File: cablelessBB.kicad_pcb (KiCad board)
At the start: 2 copper layers, 100 x 60 mm, 306 parts

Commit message: del noneed file
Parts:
- moved REF** 20.0 mm to (152.7, 46.1)
- moved REF** 20.0 mm to (152.7, 48.6)
- moved REF** 20.0 mm to (152.7, 38.5)
- moved REF** 20.0 mm to (152.7, 36.0)
- moved REF** 20.0 mm to (152.7, 41.0)
- moved REF** 20.0 mm to (152.7, 43.6)
- moved REF** 20.0 mm to (152.7, 51.2)
- moved REF** 20.0 mm to (155.2, 51.2)
- moved REF** 20.0 mm to (155.2, 43.6)
- moved REF** 20.0 mm to (155.2, 41.0)
- moved REF** 20.0 mm to (155.2, 36.0)
- moved REF** 20.0 mm to (155.2, 38.5)
- moved REF** 20.0 mm to (155.2, 48.6)
- moved REF** 20.0 mm to (155.2, 46.1)
- moved REF** 20.0 mm to (155.2, 63.9)
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
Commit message: 配線1
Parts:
- removed the REF** at (159.0, 72.8)
- removed the REF** at (161.5, 65.2)
- removed the REF** at (174.2, 32.1)
- removed the REF** at (174.2, 41.0)
- removed the REF** at (174.2, 48.6)
- removed the REF** at (174.2, 44.8)
- removed the REF** at (174.2, 51.3)
- removed the REF** at (174.2, 28.3)
- removed the REF** at (176.8, 28.3)
- removed the REF** at (176.8, 51.3)
- removed the REF** at (176.8, 44.8)
- removed the REF** at (176.8, 48.6)
- removed the REF** at (161.5, 61.4)
- removed the REF** at (176.8, 41.0)
- removed the REF** at (216.5, 58.8)
- removed the REF** at (216.5, 61.4)
- removed the REF** at (216.5, 66.4)
- removed the REF** at (216.5, 63.9)
- removed the REF** at (216.5, 74.0)
- removed the REF** at (216.5, 71.5)
- removed the REF** at (216.5, 69.0)
- removed the REF** at (216.5, 46.1)
- removed the REF** at (216.5, 48.6)
- removed the REF** at (161.5, 69.0)
- removed the REF** at (216.5, 51.2)
- removed the REF** at (216.5, 41.0)
- removed the REF** at (216.5, 43.6)
- removed the REF** at (216.5, 38.5)
- removed the REF** at (188.6, 51.2)
- removed the REF** at (188.6, 48.6)
- removed the REF** at (188.6, 44.8)
- removed the REF** at (188.6, 37.2)
- removed the REF** at (188.6, 41.0)
- removed the REF** at (188.6, 32.1)
- removed the REF** at (161.5, 77.9)
- removed the REF** at (201.3, 28.3)
- removed the REF** at (191.1, 41.0)
- removed the REF** at (191.1, 44.8)
- removed the REF** at (191.1, 48.6)
- removed the REF** at (191.1, 51.2)
- removed the REF** at (203.8, 28.3)
- removed the REF** at (191.1, 32.1)
- removed the REF** at (191.1, 37.2)
- removed the REF** at (196.2, 37.2)
- removed the REF** at (196.2, 32.1)
- removed the REF** at (161.5, 72.8)
- removed the REF** at (196.2, 51.2)
- removed the REF** at (196.2, 48.6)
- removed the REF** at (196.2, 44.8)
- removed the REF** at (196.2, 41.0)
- removed the REF** at (193.7, 32.1)
- removed the REF** at (193.7, 41.0)
- removed the REF** at (193.7, 37.2)
- removed the REF** at (193.7, 44.8)
- removed the REF** at (193.7, 48.6)
- removed the REF** at (193.7, 51.2)
- removed the REF** at (166.6, 72.8)
- removed the REF** at (203.8, 51.2)
- removed the REF** at (203.8, 48.6)
- removed the REF** at (203.8, 44.8)
- removed the REF** at (203.8, 37.2)
- removed the REF** at (203.8, 41.0)
- removed the REF** at (203.8, 32.1)
- removed the REF** at (206.4, 41.0)
- removed the REF** at (206.4, 44.8)
- removed the REF** at (206.4, 48.6)
- removed the REF** at (206.4, 51.2)
- removed the REF** at (166.6, 77.9)
- removed the REF** at (206.4, 28.3)
- removed the REF** at (206.4, 32.1)
- removed the REF** at (206.4, 37.2)
- removed the REF** at (201.3, 37.2)
- removed the REF** at (201.3, 32.1)
- removed the REF** at (201.3, 51.2)
- removed the REF** at (201.3, 48.6)
- removed the REF** at (201.3, 44.8)
- removed the REF** at (201.3, 41.0)
- removed the REF** at (198.7, 32.1)
- removed the REF** at (166.6, 69.0)
- removed the REF** at (198.7, 41.0)
- removed the REF** at (198.7, 37.2)
- removed the REF** at (198.7, 44.8)
- removed the REF** at (198.7, 48.6)
- removed the REF** at (198.7, 51.2)
- removed the REF** at (191.1, 28.3)
- removed the REF** at (193.7, 28.3)
- removed the REF** at (186.0, 37.2)
- removed the REF** at (186.0, 32.1)
- removed the REF** at (198.7, 28.3)
- removed the REF** at (166.6, 61.4)
- removed the REF** at (186.0, 51.2)
- removed the REF** at (186.0, 48.6)
- removed the REF** at (186.0, 44.8)
- removed the REF** at (186.0, 41.0)
- removed the REF** at (196.2, 28.3)
- removed the REF** at (183.5, 32.1)
- removed the REF** at (183.5, 41.0)
- removed the REF** at (183.5, 37.2)
- removed the REF** at (183.5, 44.8)
- removed the REF** at (183.5, 48.6)
- removed the REF** at (166.6, 65.2)
- removed the REF** at (183.5, 51.2)
- removed the REF** at (186.0, 28.3)
- removed the REF** at (188.6, 28.3)
- removed the REF** at (183.5, 28.3)
- removed the REF** at (188.6, 76.6)
- removed the REF** at (188.6, 80.4)
- removed the REF** at (191.1, 80.4)
- removed the REF** at (191.1, 76.6)
- removed the REF** at (196.2, 76.6)
- removed the REF** at (196.2, 80.4)
- removed the REF** at (159.0, 77.9)
- removed the REF** at (166.6, 58.7)
- removed the REF** at (193.7, 80.4)
- removed the REF** at (193.7, 76.6)
- removed the REF** at (203.8, 76.6)
- removed the REF** at (203.8, 80.4)
- removed the REF** at (206.4, 80.4)
- removed the REF** at (206.4, 76.6)
- removed the REF** at (201.3, 76.6)
- removed the REF** at (201.3, 80.4)
- removed the REF** at (198.7, 80.4)
- removed the REF** at (198.7, 76.6)
- removed the REF** at (166.6, 81.7)
- removed the REF** at (186.0, 76.6)
- removed the REF** at (186.0, 80.4)
- removed the REF** at (183.5, 80.4)
- removed the REF** at (183.5, 76.6)
- removed the REF** at (188.6, 58.8)
- removed the REF** at (188.6, 61.4)
- removed the REF** at (164.1, 81.7)
- removed the REF** at (188.6, 65.2)
- removed the REF** at (188.6, 72.8)
- removed the REF** at (188.6, 69.0)
- removed the REF** at (191.1, 69.0)
- removed the REF** at (191.1, 72.8)
- removed the REF** at (191.1, 65.2)
- removed the REF** at (191.1, 61.4)
- removed the REF** at (191.1, 58.8)
- removed the REF** at (196.2, 58.8)
- removed the REF** at (196.2, 61.4)
- removed the REF** at (164.1, 58.7)
- removed the REF** at (196.2, 65.2)
- removed the REF** at (196.2, 72.8)
- removed the REF** at (196.2, 69.0)
- removed the REF** at (193.7, 69.0)
- removed the REF** at (193.7, 72.8)
- removed the REF** at (193.7, 65.2)
- removed the REF** at (193.7, 61.4)
- removed the REF** at (193.7, 58.8)
- removed the REF** at (203.8, 58.8)
- removed the REF** at (203.8, 61.4)
- removed the REF** at (164.1, 65.2)
- removed the REF** at (203.8, 65.2)
- removed the REF** at (203.8, 72.8)
- removed the REF** at (203.8, 69.0)
- removed the REF** at (206.4, 69.0)
- removed the REF** at (206.4, 72.8)
- removed the REF** at (206.4, 65.2)
- removed the REF** at (206.4, 61.4)
- removed the REF** at (206.4, 58.8)
- removed the REF** at (201.3, 58.8)
- removed the REF** at (201.3, 61.4)
- removed the REF** at (164.1, 61.4)
- removed the REF** at (201.3, 65.2)
- removed the REF** at (201.3, 72.8)
- removed the REF** at (201.3, 69.0)
- removed the REF** at (198.7, 69.0)
- removed the REF** at (198.7, 72.8)
- removed the REF** at (198.7, 65.2)
- removed the REF** at (198.7, 61.4)
- removed the REF** at (198.7, 58.8)
- removed the REF** at (186.0, 58.8)
- removed the REF** at (186.0, 61.4)
- removed the REF** at (164.1, 69.0)
- removed the REF** at (186.0, 65.2)
- removed the REF** at (186.0, 72.8)
- removed the REF** at (186.0, 69.0)
- removed the REF** at (183.5, 69.0)
- removed the REF** at (183.5, 72.8)
- removed the REF** at (183.5, 65.2)
- removed the REF** at (183.5, 61.4)
- removed the REF** at (183.5, 58.8)
- removed the REF** at (216.5, 36.0)
- removed the REF** at (152.7, 46.1)
- removed the REF** at (164.1, 77.9)
- removed the REF** at (152.7, 48.6)
- removed the REF** at (152.7, 38.5)
- removed the REF** at (152.7, 36.0)
- removed the REF** at (152.7, 41.0)
- removed the REF** at (152.7, 43.6)
- removed the REF** at (152.7, 51.2)
- removed the REF** at (155.2, 51.2)
- removed the REF** at (155.2, 43.6)
- removed the REF** at (155.2, 41.0)
- removed the REF** at (155.2, 36.0)
- removed the REF** at (164.1, 72.8)
- removed the REF** at (155.2, 38.5)
- removed the REF** at (155.2, 48.6)
- removed the REF** at (155.2, 46.1)
- removed the REF** at (155.2, 63.9)
- removed the REF** at (155.2, 61.4)
- removed the REF** at (155.2, 71.5)
- removed the REF** at (155.2, 74.0)
- removed the REF** at (155.2, 69.0)
- removed the REF** at (155.2, 66.4)
- removed the REF** at (155.2, 58.8)
- removed the REF** at (174.2, 72.8)
- removed the REF** at (152.7, 58.8)
- removed the REF** at (152.7, 66.4)
- removed the REF** at (152.7, 69.0)
- removed the REF** at (152.7, 74.0)
- removed the REF** at (152.7, 71.5)
- removed the REF** at (152.7, 61.4)
- removed the REF** at (152.7, 63.9)
- removed the REF** at (152.7, 33.4)
- removed the REF** at (152.7, 30.9)
- removed the REF** at (155.2, 30.9)
- removed the REF** at (159.0, 69.0)
- removed the REF** at (174.2, 77.9)
- removed the REF** at (155.2, 33.4)
- removed the REF** at (155.2, 76.6)
- removed the REF** at (155.2, 79.1)
- removed the REF** at (152.7, 79.1)
- removed the REF** at (152.7, 76.6)
- removed the REF** at (176.8, 32.1)
- removed the REF** at (176.8, 37.2)
- removed the REF** at (174.2, 69.0)
- removed the REF** at (174.2, 61.4)
- removed the REF** at (174.2, 65.2)
- removed the REF** at (174.2, 58.7)
- removed the REF** at (174.2, 81.7)
- removed the REF** at (176.8, 81.7)
- removed the REF** at (176.8, 58.7)
- removed the REF** at (176.8, 65.2)
- removed the REF** at (176.8, 61.4)
- removed the REF** at (159.0, 61.4)
- removed the REF** at (176.8, 69.0)
- removed the REF** at (176.8, 77.9)
- removed the REF** at (176.8, 72.8)
- removed the REF** at (171.7, 72.8)
- removed the REF** at (171.7, 77.9)
- removed the REF** at (171.7, 69.0)
- removed the REF** at (171.7, 61.4)
- removed the REF** at (171.7, 65.2)
- removed the REF** at (171.7, 58.7)
- removed the REF** at (171.7, 81.7)
- removed the REF** at (159.0, 65.2)
- removed the REF** at (169.1, 81.7)
- removed the REF** at (169.1, 58.7)
- removed the REF** at (169.1, 65.2)
- removed the REF** at (169.1, 61.4)
- removed the REF** at (169.1, 69.0)
- removed the REF** at (169.1, 77.9)
- removed the REF** at (169.1, 72.8)
- removed the REF** at (166.6, 37.2)
- removed the REF** at (166.6, 32.1)
- removed the REF** at (166.6, 41.0)
- removed the REF** at (159.0, 58.7)
- removed the REF** at (166.6, 48.6)
- removed the REF** at (166.6, 44.8)
- removed the REF** at (166.6, 51.3)
- removed the REF** at (166.6, 28.3)
- removed the REF** at (164.1, 28.3)
- removed the REF** at (164.1, 51.3)
- removed the REF** at (164.1, 44.8)
- removed the REF** at (164.1, 48.6)
- removed the REF** at (164.1, 41.0)
- removed the REF** at (164.1, 32.1)
- removed the REF** at (159.0, 81.7)
- removed the REF** at (164.1, 37.2)
- removed the REF** at (159.0, 37.2)
- removed the REF** at (159.0, 32.1)
- removed the REF** at (159.0, 41.0)
- removed the REF** at (159.0, 48.6)
- removed the REF** at (159.0, 44.8)
- removed the REF** at (159.0, 51.3)
- removed the REF** at (159.0, 28.3)
- removed the REF** at (161.5, 28.3)
- removed the REF** at (161.5, 51.3)
- removed the REF** at (161.5, 81.7)
- removed the REF** at (161.5, 44.8)
- removed the REF** at (161.5, 48.6)
- removed the REF** at (161.5, 41.0)
- removed the REF** at (161.5, 32.1)
- removed the REF** at (161.5, 37.2)
- removed the REF** at (171.7, 37.2)
- removed the REF** at (171.7, 32.1)
- removed the REF** at (171.7, 41.0)
- removed the REF** at (171.7, 48.6)
- removed the REF** at (171.7, 44.8)
- removed the REF** at (161.5, 58.7)
- removed the REF** at (171.7, 51.3)
- removed the REF** at (171.7, 28.3)
- removed the REF** at (169.1, 28.3)
- removed the REF** at (169.1, 51.3)
- removed the REF** at (169.1, 44.8)
- removed the REF** at (169.1, 48.6)
- removed the REF** at (169.1, 41.0)
- removed the REF** at (169.1, 32.1)
- removed the REF** at (169.1, 37.2)
- removed the REF** at (174.2, 37.2)
- added JP1: Jumper_NO_Small, lib:jump, F.Cu at (110.2, 55.5)
- added JP10: Jumper_NO_Small, lib:jump, F.Cu at (110.2, 124.1)
- added JP100: Jumper_NO_Small, lib:jump, F.Cu at (125.4, 63.2)
- added JP101: Jumper_NO_Small, lib:jump, F.Cu at (125.4, 65.7)
- added JP102: Jumper_NO_Small, lib:jump, F.Cu at (125.4, 68.2)
- added JP103: Jumper_NO_Small, lib:jump, F.Cu at (125.4, 75.9)
- added JP104: Jumper_NO_Small, lib:jump, F.Cu at (125.4, 81.0)
- added JP105: Jumper_NO_Small, lib:jump, F.Cu at (125.4, 119.0)
- added JP106: Jumper_NO_Small, lib:jump, F.Cu at (125.4, 124.1)
- added JP107: Jumper_NO_Small, lib:jump, F.Cu at (125.4, 131.8)
- added JP108: Jumper_NO_Small, lib:jump, F.Cu at (125.4, 134.3)
- added JP109: Jumper_NO_Small, lib:jump, F.Cu at (125.4, 136.8)
- added JP11: Jumper_NO_Small, lib:jump, F.Cu at (110.2, 131.8)
- added JP110: Jumper_NO_Small, lib:jump, F.Cu at (125.4, 139.4)
- added JP111: Jumper_NO_Small, lib:jump, F.Cu at (125.4, 141.9)
- added JP112: Jumper_NO_Small, lib:jump, F.Cu at (125.4, 144.4)
- added JP113: Jumper_NO_Small, lib:jump, F.Cu at (127.9, 55.5)
- added JP114: Jumper_NO_Small, lib:jump, F.Cu at (127.9, 58.1)
- added JP115: Jumper_NO_Small, lib:jump, F.Cu at (127.9, 60.6)
- added JP116: Jumper_NO_Small, lib:jump, F.Cu at (127.9, 63.2)
- added JP117: Jumper_NO_Small, lib:jump, F.Cu at (127.9, 65.7)
- added JP118: Jumper_NO_Small, lib:jump, F.Cu at (127.9, 68.2)
- added JP119: Jumper_NO_Small, lib:jump, F.Cu at (127.9, 75.9)
- added JP12: Jumper_NO_Small, lib:jump, F.Cu at (110.2, 134.3)
- added JP120: Jumper_NO_Small, lib:jump, F.Cu at (127.9, 81.0)
- added JP121: Jumper_NO_Small, lib:jump, F.Cu at (127.9, 119.0)
- added JP122: Jumper_NO_Small, lib:jump, F.Cu at (127.9, 124.1)
- added JP123: Jumper_NO_Small, lib:jump, F.Cu at (127.9, 131.8)
- added JP124: Jumper_NO_Small, lib:jump, F.Cu at (127.9, 134.3)
- added JP125: Jumper_NO_Small, lib:jump, F.Cu at (127.9, 136.8)
- added JP126: Jumper_NO_Small, lib:jump, F.Cu at (127.9, 139.4)
- added JP127: Jumper_NO_Small, lib:jump, F.Cu at (127.9, 141.9)
- added JP128: Jumper_NO_Small, lib:jump, F.Cu at (127.9, 144.4)
- added JP129: Jumper_NO_Small, lib:jump, F.Cu at (130.5, 55.5)
- added JP13: Jumper_NO_Small, lib:jump, F.Cu at (110.2, 136.8)
- added JP130: Jumper_NO_Small, lib:jump, F.Cu at (130.5, 58.1)
- added JP131: Jumper_NO_Small, lib:jump, F.Cu at (130.5, 60.6)
- added JP132: Jumper_NO_Small, lib:jump, F.Cu at (130.5, 63.2)
- added JP133: Jumper_NO_Small, lib:jump, F.Cu at (130.5, 65.7)
- added JP134: Jumper_NO_Small, lib:jump, F.Cu at (130.5, 68.2)
- added JP135: Jumper_NO_Small, lib:jump, F.Cu at (130.5, 75.9)
- added JP136: Jumper_NO_Small, lib:jump, F.Cu at (130.5, 81.0)
- added JP137: Jumper_NO_Small, lib:jump, F.Cu at (130.5, 119.0)
- added JP138: Jumper_NO_Small, lib:jump, F.Cu at (130.5, 124.1)
- added JP139: Jumper_NO_Small, lib:jump, F.Cu at (130.5, 131.8)
- added JP14: Jumper_NO_Small, lib:jump, F.Cu at (110.2, 139.4)
- added JP140: Jumper_NO_Small, lib:jump, F.Cu at (130.5, 134.3)
- added JP141: Jumper_NO_Small, lib:jump, F.Cu at (130.5, 136.8)
- added JP142: Jumper_NO_Small, lib:jump, F.Cu at (130.5, 139.4)
- added JP143: Jumper_NO_Small, lib:jump, F.Cu at (130.5, 141.9)
- added JP144: Jumper_NO_Small, lib:jump, F.Cu at (130.5, 144.4)
- added JP145: Jumper_NO_Small, lib:jump, F.Cu at (133.0, 55.5)
- added JP146: Jumper_NO_Small, lib:jump, F.Cu at (133.0, 58.1)
- added JP147: Jumper_NO_Small, lib:jump, F.Cu at (133.0, 60.6)
- added JP148: Jumper_NO_Small, lib:jump, F.Cu at (133.0, 63.2)
- added JP149: Jumper_NO_Small, lib:jump, F.Cu at (133.0, 65.7)
- added JP15: Jumper_NO_Small, lib:jump, F.Cu at (110.2, 141.9)
- added JP150: Jumper_NO_Small, lib:jump, F.Cu at (133.0, 68.2)
- added JP151: Jumper_NO_Small, lib:jump, F.Cu at (133.0, 75.9)
- added JP152: Jumper_NO_Small, lib:jump, F.Cu at (133.0, 81.0)
- added JP153: Jumper_NO_Small, lib:jump, F.Cu at (133.0, 119.0)
- added JP154: Jumper_NO_Small, lib:jump, F.Cu at (133.0, 124.1)
- added JP155: Jumper_NO_Small, lib:jump, F.Cu at (133.0, 131.8)
- added JP156: Jumper_NO_Small, lib:jump, F.Cu at (133.0, 134.3)
- added JP157: Jumper_NO_Small, lib:jump, F.Cu at (133.0, 136.8)
- added JP158: Jumper_NO_Small, lib:jump, F.Cu at (133.0, 139.4)
- added JP159: Jumper_NO_Small, lib:jump, F.Cu at (133.0, 141.9)
- added JP16: Jumper_NO_Small, lib:jump, F.Cu at (110.2, 144.4)
- added JP160: Jumper_NO_Small, lib:jump, F.Cu at (133.0, 144.4)
- added JP161: Jumper_NO_Small, lib:jump, F.Cu at (135.6, 55.5)
- added JP162: Jumper_NO_Small, lib:jump, F.Cu at (135.6, 58.1)
- added JP163: Jumper_NO_Small, lib:jump, F.Cu at (135.6, 60.6)
- added JP164: Jumper_NO_Small, lib:jump, F.Cu at (135.6, 63.2)
- added JP165: Jumper_NO_Small, lib:jump, F.Cu at (135.6, 65.7)
- added JP166: Jumper_NO_Small, lib:jump, F.Cu at (135.6, 68.2)
- added JP167: Jumper_NO_Small, lib:jump, F.Cu at (135.6, 75.9)
- added JP168: Jumper_NO_Small, lib:jump, F.Cu at (135.6, 81.0)
- added JP169: Jumper_NO_Small, lib:jump, F.Cu at (135.6, 119.0)
- added JP17: Jumper_NO_Small, lib:jump, F.Cu at (112.7, 55.5)
- added JP170: Jumper_NO_Small, lib:jump, F.Cu at (135.6, 124.1)
- added JP171: Jumper_NO_Small, lib:jump, F.Cu at (135.6, 131.8)
- added JP172: Jumper_NO_Small, lib:jump, F.Cu at (135.6, 134.3)
- added JP173: Jumper_NO_Small, lib:jump, F.Cu at (135.6, 136.8)
- added JP174: Jumper_NO_Small, lib:jump, F.Cu at (135.6, 139.4)
- added JP175: Jumper_NO_Small, lib:jump, F.Cu at (135.6, 141.9)
- added JP176: Jumper_NO_Small, lib:jump, F.Cu at (135.6, 144.4)
- added JP177: Jumper_NO_Small, lib:jump, F.Cu at (138.1, 55.5)
- added JP178: Jumper_NO_Small, lib:jump, F.Cu at (138.1, 58.1)
- added JP179: Jumper_NO_Small, lib:jump, F.Cu at (138.1, 60.6)
- added JP18: Jumper_NO_Small, lib:jump, F.Cu at (112.7, 58.1)
- added JP180: Jumper_NO_Small, lib:jump, F.Cu at (138.1, 63.2)
- added JP181: Jumper_NO_Small, lib:jump, F.Cu at (138.1, 65.7)
- added JP182: Jumper_NO_Small, lib:jump, F.Cu at (138.1, 68.2)
- added JP183: Jumper_NO_Small, lib:jump, F.Cu at (138.1, 75.9)
- added JP184: Jumper_NO_Small, lib:jump, F.Cu at (138.1, 81.0)
- added JP185: Jumper_NO_Small, lib:jump, F.Cu at (138.1, 119.0)
- added JP186: Jumper_NO_Small, lib:jump, F.Cu at (138.1, 124.1)
- added JP187: Jumper_NO_Small, lib:jump, F.Cu at (138.1, 131.8)
- added JP188: Jumper_NO_Small, lib:jump, F.Cu at (138.1, 134.3)
- added JP189: Jumper_NO_Small, lib:jump, F.Cu at (138.1, 136.8)
- added JP19: Jumper_NO_Small, lib:jump, F.Cu at (112.7, 60.6)
- added JP190: Jumper_NO_Small, lib:jump, F.Cu at (138.1, 139.4)
- added JP191: Jumper_NO_Small, lib:jump, F.Cu at (138.1, 141.9)
- added JP192: Jumper_NO_Small, lib:jump, F.Cu at (138.1, 144.4)
- added JP193: Jumper_NO_Small, lib:jump, F.Cu at (140.6, 55.5)
- added JP194: Jumper_NO_Small, lib:jump, F.Cu at (140.6, 58.1)
- added JP195: Jumper_NO_Small, lib:jump, F.Cu at (140.6, 60.6)
- added JP196: Jumper_NO_Small, lib:jump, F.Cu at (140.6, 63.2)
- added JP197: Jumper_NO_Small, lib:jump, F.Cu at (140.6, 65.7)
- added JP198: Jumper_NO_Small, lib:jump, F.Cu at (140.6, 68.2)
- added JP199: Jumper_NO_Small, lib:jump, F.Cu at (140.6, 75.9)
- added JP2: Jumper_NO_Small, lib:jump, F.Cu at (110.2, 58.1)
- added JP20: Jumper_NO_Small, lib:jump, F.Cu at (112.7, 63.2)
- added JP200: Jumper_NO_Small, lib:jump, F.Cu at (140.6, 81.0)
- added JP201: Jumper_NO_Small, lib:jump, F.Cu at (140.6, 119.0)
- added JP202: Jumper_NO_Small, lib:jump, F.Cu at (140.6, 124.1)
- added JP203: Jumper_NO_Small, lib:jump, F.Cu at (140.6, 131.8)
- added JP204: Jumper_NO_Small, lib:jump, F.Cu at (140.6, 134.3)
- added JP205: Jumper_NO_Small, lib:jump, F.Cu at (140.6, 136.8)
- added JP206: Jumper_NO_Small, lib:jump, F.Cu at (140.6, 139.4)
- added JP207: Jumper_NO_Small, lib:jump, F.Cu at (140.6, 141.9)
- added JP208: Jumper_NO_Small, lib:jump, F.Cu at (140.6, 144.4)
- added JP209: Jumper_NO_Small, lib:jump, F.Cu at (143.2, 55.5)
- added JP21: Jumper_NO_Small, lib:jump, F.Cu at (112.7, 65.7)
- added JP210: Jumper_NO_Small, lib:jump, F.Cu at (143.2, 58.1)
- added JP211: Jumper_NO_Small, lib:jump, F.Cu at (143.2, 60.6)
- added JP212: Jumper_NO_Small, lib:jump, F.Cu at (143.2, 63.2)
- added JP213: Jumper_NO_Small, lib:jump, F.Cu at (143.2, 65.7)
- added JP214: Jumper_NO_Small, lib:jump, F.Cu at (143.2, 68.2)
- added JP215: Jumper_NO_Small, lib:jump, F.Cu at (143.2, 75.9)
- added JP216: Jumper_NO_Small, lib:jump, F.Cu at (143.2, 81.0)
- added JP217: Jumper_NO_Small, lib:jump, F.Cu at (143.2, 119.0)
- added JP218: Jumper_NO_Small, lib:jump, F.Cu at (143.2, 124.1)
- added JP219: Jumper_NO_Small, lib:jump, F.Cu at (143.2, 131.8)
- added JP22: Jumper_NO_Small, lib:jump, F.Cu at (112.7, 68.2)
- added JP220: Jumper_NO_Small, lib:jump, F.Cu at (143.2, 134.3)
- added JP221: Jumper_NO_Small, lib:jump, F.Cu at (143.2, 136.8)
- added JP222: Jumper_NO_Small, lib:jump, F.Cu at (143.2, 139.4)
- added JP223: Jumper_NO_Small, lib:jump, F.Cu at (143.2, 141.9)
- added JP224: Jumper_NO_Small, lib:jump, F.Cu at (143.2, 144.4)
- added JP225: Jumper_NO_Small, lib:jump, F.Cu at (145.7, 55.5)
- added JP226: Jumper_NO_Small, lib:jump, F.Cu at (145.7, 58.1)
- added JP227: Jumper_NO_Small, lib:jump, F.Cu at (145.7, 60.6)
- added JP228: Jumper_NO_Small, lib:jump, F.Cu at (145.7, 63.2)
- added JP229: Jumper_NO_Small, lib:jump, F.Cu at (145.7, 65.7)
- added JP23: Jumper_NO_Small, lib:jump, F.Cu at (112.7, 75.9)
- added JP230: Jumper_NO_Small, lib:jump, F.Cu at (145.7, 68.2)
- added JP231: Jumper_NO_Small, lib:jump, F.Cu at (145.7, 75.9)
- added JP232: Jumper_NO_Small, lib:jump, F.Cu at (145.7, 81.0)
- added JP233: Jumper_NO_Small, lib:jump, F.Cu at (145.7, 119.0)
- added JP234: Jumper_NO_Small, lib:jump, F.Cu at (145.7, 124.1)
- added JP235: Jumper_NO_Small, lib:jump, F.Cu at (145.7, 131.8)
- added JP236: Jumper_NO_Small, lib:jump, F.Cu at (145.7, 134.3)
- added JP237: Jumper_NO_Small, lib:jump, F.Cu at (145.7, 136.8)
- added JP238: Jumper_NO_Small, lib:jump, F.Cu at (145.7, 139.4)
- added JP239: Jumper_NO_Small, lib:jump, F.Cu at (145.7, 141.9)
- added JP24: Jumper_NO_Small, lib:jump, F.Cu at (112.7, 81.0)
- added JP240: Jumper_NO_Small, lib:jump, F.Cu at (145.7, 144.4)
- added JP25: Jumper_NO_Small, lib:jump, F.Cu at (112.7, 119.0)
- added JP26: Jumper_NO_Small, lib:jump, F.Cu at (112.7, 124.1)
- added JP27: Jumper_NO_Small, lib:jump, F.Cu at (112.7, 131.8)
- added JP28: Jumper_NO_Small, lib:jump, F.Cu at (112.7, 134.3)
- added JP29: Jumper_NO_Small, lib:jump, F.Cu at (112.7, 136.8)
- added JP3: Jumper_NO_Small, lib:jump, F.Cu at (110.2, 60.6)
- added JP30: Jumper_NO_Small, lib:jump, F.Cu at (112.7, 139.4)
- added JP31: Jumper_NO_Small, lib:jump, F.Cu at (112.7, 141.9)
- added JP32: Jumper_NO_Small, lib:jump, F.Cu at (112.7, 144.4)
- added JP33: Jumper_NO_Small, lib:jump, F.Cu at (115.2, 55.5)
- added JP34: Jumper_NO_Small, lib:jump, F.Cu at (115.2, 58.1)
- added JP35: Jumper_NO_Small, lib:jump, F.Cu at (115.2, 60.6)
- added JP36: Jumper_NO_Small, lib:jump, F.Cu at (115.2, 63.2)
- added JP37: Jumper_NO_Small, lib:jump, F.Cu at (115.2, 65.7)
- added JP38: Jumper_NO_Small, lib:jump, F.Cu at (115.2, 68.2)
- added JP39: Jumper_NO_Small, lib:jump, F.Cu at (115.2, 75.9)
- added JP4: Jumper_NO_Small, lib:jump, F.Cu at (110.2, 63.2)
- added JP40: Jumper_NO_Small, lib:jump, F.Cu at (115.2, 81.0)
- added JP41: Jumper_NO_Small, lib:jump, F.Cu at (115.2, 119.0)
- added JP42: Jumper_NO_Small, lib:jump, F.Cu at (115.2, 124.1)
- added JP43: Jumper_NO_Small, lib:jump, F.Cu at (115.2, 131.8)
- added JP44: Jumper_NO_Small, lib:jump, F.Cu at (115.2, 134.3)
- added JP45: Jumper_NO_Small, lib:jump, F.Cu at (115.2, 136.8)
- added JP46: Jumper_NO_Small, lib:jump, F.Cu at (115.2, 139.4)
- added JP47: Jumper_NO_Small, lib:jump, F.Cu at (115.2, 141.9)
- added JP48: Jumper_NO_Small, lib:jump, F.Cu at (115.2, 144.4)
- added JP49: Jumper_NO_Small, lib:jump, F.Cu at (117.8, 55.5)
- added JP5: Jumper_NO_Small, lib:jump, F.Cu at (110.2, 65.7)
- added JP50: Jumper_NO_Small, lib:jump, F.Cu at (117.8, 58.1)
- added JP51: Jumper_NO_Small, lib:jump, F.Cu at (117.8, 60.6)
- added JP52: Jumper_NO_Small, lib:jump, F.Cu at (117.8, 63.2)
- added JP53: Jumper_NO_Small, lib:jump, F.Cu at (117.8, 65.7)
- added JP54: Jumper_NO_Small, lib:jump, F.Cu at (117.8, 68.2)
- added JP55: Jumper_NO_Small, lib:jump, F.Cu at (117.8, 75.9)
- added JP56: Jumper_NO_Small, lib:jump, F.Cu at (117.8, 81.0)
- added JP57: Jumper_NO_Small, lib:jump, F.Cu at (117.8, 119.0)
- added JP58: Jumper_NO_Small, lib:jump, F.Cu at (117.8, 124.1)
- added JP59: Jumper_NO_Small, lib:jump, F.Cu at (117.8, 131.8)
- added JP6: Jumper_NO_Small, lib:jump, F.Cu at (110.2, 68.2)
- added JP60: Jumper_NO_Small, lib:jump, F.Cu at (117.8, 134.3)
- added JP61: Jumper_NO_Small, lib:jump, F.Cu at (117.8, 136.8)
- added JP62: Jumper_NO_Small, lib:jump, F.Cu at (117.8, 139.4)
- added JP63: Jumper_NO_Small, lib:jump, F.Cu at (117.8, 141.9)
- added JP64: Jumper_NO_Small, lib:jump, F.Cu at (117.8, 144.4)
- added JP65: Jumper_NO_Small, lib:jump, F.Cu at (120.3, 55.5)
- added JP66: Jumper_NO_Small, lib:jump, F.Cu at (120.3, 58.1)
- added JP67: Jumper_NO_Small, lib:jump, F.Cu at (120.3, 60.6)
- added JP68: Jumper_NO_Small, lib:jump, F.Cu at (120.3, 63.2)
- added JP69: Jumper_NO_Small, lib:jump, F.Cu at (120.3, 65.7)
- added JP7: Jumper_NO_Small, lib:jump, F.Cu at (110.2, 75.9)
- added JP70: Jumper_NO_Small, lib:jump, F.Cu at (120.3, 68.2)
- added JP71: Jumper_NO_Small, lib:jump, F.Cu at (120.3, 75.9)
- added JP72: Jumper_NO_Small, lib:jump, F.Cu at (120.3, 81.0)
- added JP73: Jumper_NO_Small, lib:jump, F.Cu at (120.3, 119.0)
- added JP74: Jumper_NO_Small, lib:jump, F.Cu at (120.3, 124.1)
- added JP75: Jumper_NO_Small, lib:jump, F.Cu at (120.3, 131.8)
- added JP76: Jumper_NO_Small, lib:jump, F.Cu at (120.3, 134.3)
- added JP77: Jumper_NO_Small, lib:jump, F.Cu at (120.3, 136.8)
- added JP78: Jumper_NO_Small, lib:jump, F.Cu at (120.3, 139.4)
- added JP79: Jumper_NO_Small, lib:jump, F.Cu at (120.3, 141.9)
- added JP8: Jumper_NO_Small, lib:jump, F.Cu at (110.2, 81.0)
- added JP80: Jumper_NO_Small, lib:jump, F.Cu at (120.3, 144.4)
- added JP81: Jumper_NO_Small, lib:jump, F.Cu at (122.9, 55.5)
- added JP82: Jumper_NO_Small, lib:jump, F.Cu at (122.9, 58.1)
- added JP83: Jumper_NO_Small, lib:jump, F.Cu at (122.9, 60.6)
- added JP84: Jumper_NO_Small, lib:jump, F.Cu at (122.9, 63.2)
- added JP85: Jumper_NO_Small, lib:jump, F.Cu at (122.9, 65.7)
- added JP86: Jumper_NO_Small, lib:jump, F.Cu at (122.9, 68.2)
- added JP87: Jumper_NO_Small, lib:jump, F.Cu at (122.9, 75.9)
- added JP88: Jumper_NO_Small, lib:jump, F.Cu at (122.9, 81.0)
- added JP89: Jumper_NO_Small, lib:jump, F.Cu at (122.9, 119.0)
- added JP9: Jumper_NO_Small, lib:jump, F.Cu at (110.2, 119.0)
- added JP90: Jumper_NO_Small, lib:jump, F.Cu at (122.9, 124.1)
- added JP91: Jumper_NO_Small, lib:jump, F.Cu at (122.9, 131.8)
- added JP92: Jumper_NO_Small, lib:jump, F.Cu at (122.9, 134.3)
- added JP93: Jumper_NO_Small, lib:jump, F.Cu at (122.9, 136.8)
- added JP94: Jumper_NO_Small, lib:jump, F.Cu at (122.9, 139.4)
- added JP95: Jumper_NO_Small, lib:jump, F.Cu at (122.9, 141.9)
- added JP96: Jumper_NO_Small, lib:jump, F.Cu at (122.9, 144.4)
- added JP97: Jumper_NO_Small, lib:jump, F.Cu at (125.4, 55.5)
- added JP98: Jumper_NO_Small, lib:jump, F.Cu at (125.4, 58.1)
- added JP99: Jumper_NO_Small, lib:jump, F.Cu at (125.4, 60.6)
- added P1: CONN_01X06, Pin_Headers:Pin_Header_Straight_1x06_Pitch2.54mm, F.Cu at (105.1, 73.3)
- added P10: CONN_01X06, lib:6p, F.Cu at (112.7, 116.5)
- added P11: CONN_01X02, lib:2P, F.Cu at (112.7, 73.3)
- added P12: CONN_01X02, lib:2P, F.Cu at (112.7, 126.7)
- added P13: CONN_01X06, lib:6p, F.Cu at (115.2, 96.2)
- added P14: CONN_01X06, lib:6p, F.Cu at (115.2, 116.5)
- added P15: CONN_01X02, lib:2P, F.Cu at (115.2, 73.3)
- added P16: CONN_01X02, lib:2P, F.Cu at (115.2, 126.7)
- added P17: CONN_01X06, lib:6p, F.Cu at (117.8, 96.2)
- added P18: CONN_01X06, lib:6p, F.Cu at (117.8, 116.5)
- added P19: CONN_01X02, lib:2P, F.Cu at (117.8, 73.3)
- added P2: CONN_01X02, Pin_Headers:Pin_Header_Straight_1x02_Pitch2.54mm, F.Cu at (105.1, 81.0)
- added P20: CONN_01X02, lib:2P, F.Cu at (117.8, 126.7)
- added P21: CONN_01X06, lib:6p, F.Cu at (120.3, 96.2)
- added P22: CONN_01X06, lib:6p, F.Cu at (120.3, 116.5)
- added P23: CONN_01X02, lib:2P, F.Cu at (120.3, 73.3)
- added P24: CONN_01X02, lib:2P, F.Cu at (120.3, 126.7)
- added P25: CONN_01X06, lib:6p, F.Cu at (122.9, 96.2)
- added P26: CONN_01X06, lib:6p, F.Cu at (122.9, 116.5)
- added P27: CONN_01X02, lib:2P, F.Cu at (122.9, 73.3)
- added P28: CONN_01X02, lib:2P, F.Cu at (122.9, 126.7)
- added P29: CONN_01X06, lib:6p, F.Cu at (125.4, 96.2)
- added P3: CONN_01X02, Pin_Headers:Pin_Header_Straight_1x02_Pitch2.54mm, F.Cu at (105.1, 119.0)
- added P30: CONN_01X06, lib:6p, F.Cu at (125.4, 116.5)
- added P31: CONN_01X02, lib:2P, F.Cu at (125.4, 73.3)
- added P32: CONN_01X02, lib:2P, F.Cu at (125.4, 126.7)
- added P33: CONN_01X06, lib:6p, F.Cu at (127.9, 96.2)
- added P34: CONN_01X06, lib:6p, F.Cu at (127.9, 116.5)
- added P35: CONN_01X02, lib:2P, F.Cu at (127.9, 73.3)
- added P36: CONN_01X02, lib:2P, F.Cu at (127.9, 126.7)
- added P37: CONN_01X06, lib:6p, F.Cu at (130.5, 96.2)
- added P38: CONN_01X06, lib:6p, F.Cu at (130.5, 116.5)
- added P39: CONN_01X02, lib:2P, F.Cu at (130.5, 73.3)
- added P4: CONN_01X06, Pin_Headers:Pin_Header_Straight_1x06_Pitch2.54mm, F.Cu at (105.1, 126.7)
- added P40: CONN_01X02, lib:2P, F.Cu at (130.5, 126.7)
- added P41: CONN_01X06, lib:6p, F.Cu at (133.0, 96.2)
- added P42: CONN_01X06, lib:6p, F.Cu at (133.0, 116.5)
- added P43: CONN_01X02, lib:2P, F.Cu at (133.0, 73.3)
- added P44: CONN_01X02, lib:2P, F.Cu at (133.0, 126.7)
- added P45: CONN_01X06, lib:6p, F.Cu at (135.6, 96.2)
- added P46: CONN_01X06, lib:6p, F.Cu at (135.6, 116.5)
- added P47: CONN_01X02, lib:2P, F.Cu at (135.6, 73.3)
- added P48: CONN_01X02, lib:2P, F.Cu at (135.6, 126.7)
- added P49: CONN_01X06, lib:6p, F.Cu at (138.1, 96.2)
- added P5: CONN_01X06, lib:6p, F.Cu at (110.2, 96.2)
- added P50: CONN_01X06, lib:6p, F.Cu at (138.1, 116.5)
- added P51: CONN_01X02, lib:2P, F.Cu at (138.1, 73.3)
- added P52: CONN_01X02, lib:2P, F.Cu at (138.1, 126.7)
- added P53: CONN_01X06, lib:6p, F.Cu at (140.6, 96.2)
- added P54: CONN_01X06, lib:6p, F.Cu at (140.6, 116.5)
- added P55: CONN_01X02, lib:2P, F.Cu at (140.6, 73.3)
- added P56: CONN_01X02, lib:2P, F.Cu at (140.6, 126.7)
- added P57: CONN_01X06, lib:6p, F.Cu at (143.2, 96.2)
- added P58: CONN_01X06, lib:6p, F.Cu at (143.2, 116.5)
- added P59: CONN_01X02, lib:2P, F.Cu at (143.2, 73.3)
- added P6: CONN_01X06, lib:6p, F.Cu at (110.2, 116.5)
- added P60: CONN_01X02, lib:2P, F.Cu at (143.2, 126.7)
- added P61: CONN_01X06, lib:6p, F.Cu at (145.7, 96.2)
- added P62: CONN_01X06, lib:6p, F.Cu at (145.7, 116.5)
- added P63: CONN_01X02, lib:2P, F.Cu at (145.7, 73.3)
- added P64: CONN_01X02, lib:2P, F.Cu at (145.7, 126.7)
- added P7: CONN_01X02, lib:2P, F.Cu at (110.2, 73.3)
- added P8: CONN_01X02, lib:2P, F.Cu at (110.2, 126.7)
- added P9: CONN_01X06, lib:6p, F.Cu at (112.7, 96.2)
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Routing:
- net GND: track 2229.4 -> 156.3 mm, vias 72 -> 0
- net VCC: track 0.00 -> 148.1 mm
- net Net-(JP233-Pad2): track 0.00 -> 55.2 mm, vias 0 -> 8
- net Net-(JP185-Pad2): track 0.00 -> 55.2 mm, vias 0 -> 8
- net Net-(JP177-Pad2): track 0.00 -> 55.2 mm, vias 0 -> 8
- net Net-(JP137-Pad2): track 0.00 -> 55.2 mm, vias 0 -> 8
- net Net-(JP129-Pad2): track 0.00 -> 55.2 mm, vias 0 -> 8
- net Net-(JP225-Pad2): track 0.00 -> 55.2 mm, vias 0 -> 8
- net Net-(JP73-Pad2): track 0.00 -> 55.2 mm, vias 0 -> 8
- net Net-(JP65-Pad2): track 0.00 -> 55.2 mm, vias 0 -> 8
- net Net-(JP41-Pad2): track 0.00 -> 55.2 mm, vias 0 -> 8
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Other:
- board size 100 x 60 mm -> 100 x 100 mm
- net class AC100V removed
- net class Default: clearance 0.2 -> 0.19; via_drill 0.4 -> 0.3
- net class VCC removed
- net class vm5V removed
- rule trace_clearance: 0.2 -> 0.19
- board text removed: "0"
- board text removed: "1"
- board text removed: "2"
- board text removed: "3"
- board text removed: "4"
- board text removed: "5"
- board text removed: "6"
- board text removed: "7"
- board text removed: "8"
- board text removed: "9"
- board text removed: "GND"
- board text removed: "VCC"

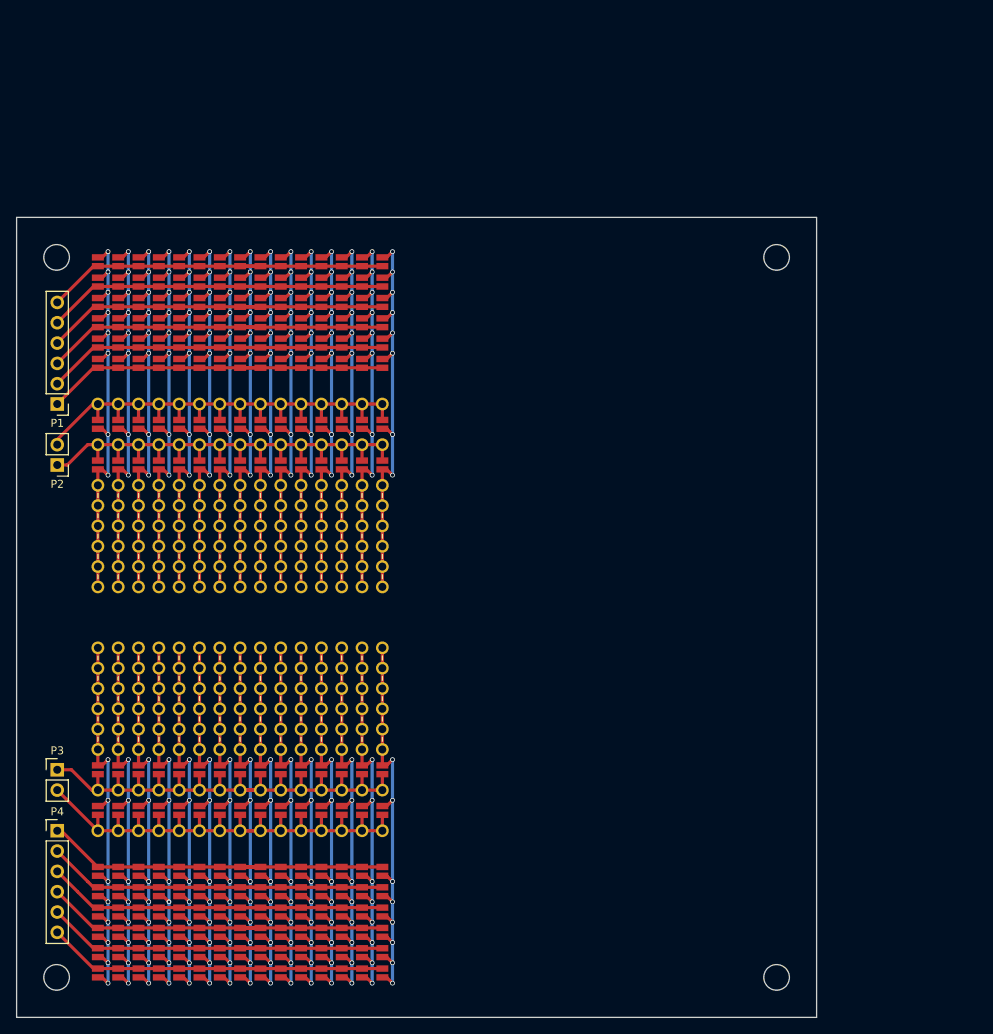
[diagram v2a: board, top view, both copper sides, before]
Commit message: add arduinoPCB
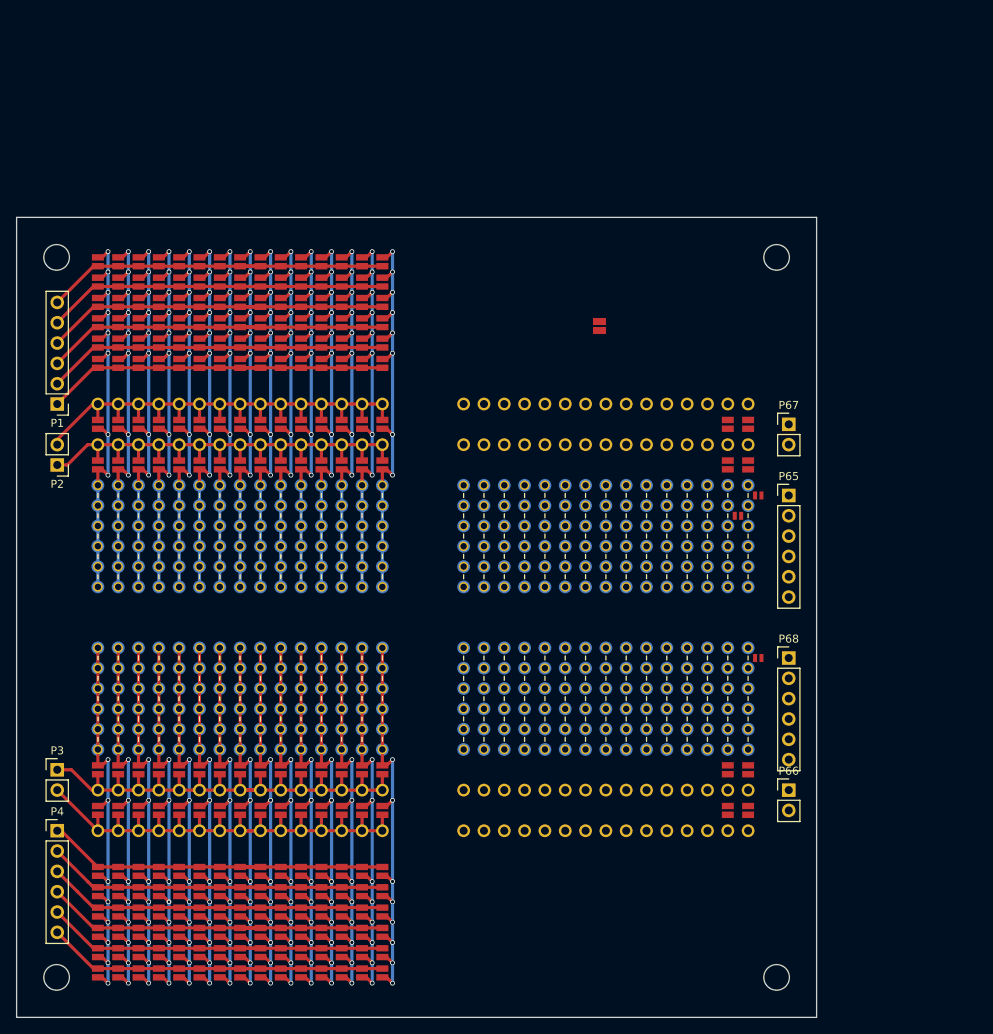
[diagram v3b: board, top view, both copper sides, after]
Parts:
- added JP241: Jumper_NO_Small, lib:j-mini, F.Cu at (192.7, 84.8)
- added JP242: Jumper_NO_Small, lib:jump, F.Cu at (191.4, 75.9)
- added JP243: Jumper_NO_Small, lib:jump, F.Cu at (191.4, 81.0)
- added JP244: Jumper_NO_Small, lib:jump, F.Cu at (191.4, 119.0)
- added JP245: Jumper_NO_Small, lib:jump, F.Cu at (191.4, 124.1)
- added JP246: Jumper_NO_Small, lib:j-mini, F.Cu at (192.7, 105.1)
- added JP247: Jumper_NO_Small, lib:j-mini, F.Cu at (190.2, 87.3)
- added JP248: Jumper_NO_Small, lib:jump, F.Cu at (188.9, 75.9)
- added JP249: Jumper_NO_Small, lib:jump, F.Cu at (188.9, 81.0)
- added JP250: Jumper_NO_Small, lib:jump, F.Cu at (188.9, 119.0)
- added JP251: Jumper_NO_Small, lib:jump, F.Cu at (188.9, 124.1)
- added JP252, JP253, JP258, JP259, JP264, JP265, JP270, JP271, JP276, JP277, JP282, JP283, JP288, JP289, JP294, JP295, JP300, JP301, JP306, JP307, JP312, JP313, JP318, JP319, JP324, JP325, JP330: Jumper_NO_Small, lib:j-mini, F.Cu at (172.9, 63.6)
- added JP254, JP255, JP256, JP257, JP260, JP261, JP262, JP263, JP266, JP267, JP268, JP269, JP272, JP273, JP274, JP275, JP278, JP279, JP280, JP281, JP284, JP285, JP286, JP287, JP290, JP291, JP292, JP293, JP296, JP297, JP298, JP299, JP302, JP303, JP304, JP305, JP308, JP309, JP310, JP311, JP314, JP315, JP316, JP317, JP320, JP321, JP322, JP323, JP326, JP327, JP328, JP329: Jumper_NO_Small, lib:jump, F.Cu at (172.9, 63.6)
- added P100: CONN_01X02, lib:2P, F.Cu at (173.7, 126.7)
- added P101: CONN_01X06, lib:6p, F.Cu at (171.1, 96.2)
- added P102: CONN_01X06, lib:6p, F.Cu at (171.1, 116.5)
- added P103: CONN_01X02, lib:2P, F.Cu at (171.1, 73.3)
- added P104: CONN_01X02, lib:2P, F.Cu at (171.1, 126.7)
- added P105: CONN_01X06, lib:6p, F.Cu at (168.6, 96.2)
- added P106: CONN_01X06, lib:6p, F.Cu at (168.6, 116.5)
- added P107: CONN_01X02, lib:2P, F.Cu at (168.6, 73.3)
- added P108: CONN_01X02, lib:2P, F.Cu at (168.6, 126.7)
- added P109: CONN_01X06, lib:6p, F.Cu at (166.0, 96.2)
- added P110: CONN_01X06, lib:6p, F.Cu at (166.0, 116.5)
- added P111: CONN_01X02, lib:2P, F.Cu at (166.0, 73.3)
- added P112: CONN_01X02, lib:2P, F.Cu at (166.0, 126.7)
- added P113: CONN_01X06, lib:6p, F.Cu at (163.5, 96.2)
- added P114: CONN_01X06, lib:6p, F.Cu at (163.5, 116.5)
- added P115: CONN_01X02, lib:2P, F.Cu at (163.5, 73.3)
- added P116: CONN_01X02, lib:2P, F.Cu at (163.5, 126.7)
- added P117: CONN_01X06, lib:6p, F.Cu at (161.0, 96.2)
- added P118: CONN_01X06, lib:6p, F.Cu at (161.0, 116.5)
- added P119: CONN_01X02, lib:2P, F.Cu at (161.0, 73.3)
- added P120: CONN_01X02, lib:2P, F.Cu at (161.0, 126.7)
- added P121: CONN_01X06, lib:6p, F.Cu at (158.4, 96.2)
- added P122: CONN_01X06, lib:6p, F.Cu at (158.4, 116.5)
- added P123: CONN_01X02, lib:2P, F.Cu at (158.4, 73.3)
- added P124: CONN_01X02, lib:2P, F.Cu at (158.4, 126.7)
- added P125: CONN_01X06, lib:6p, F.Cu at (155.9, 96.2)
- added P126: CONN_01X06, lib:6p, F.Cu at (155.9, 116.5)
- added P127: CONN_01X02, lib:2P, F.Cu at (155.9, 73.3)
- added P128: CONN_01X02, lib:2P, F.Cu at (155.9, 126.7)
- added P65: CONN_01X06, Pin_Headers:Pin_Header_Straight_1x06_Pitch2.54mm, F.Cu at (196.5, 84.8)
- added P66: CONN_01X02, Pin_Headers:Pin_Header_Straight_1x02_Pitch2.54mm, F.Cu at (196.5, 121.6)
- added P67: CONN_01X02, Pin_Headers:Pin_Header_Straight_1x02_Pitch2.54mm, F.Cu at (196.5, 75.9)
- added P68: CONN_01X06, Pin_Headers:Pin_Header_Straight_1x06_Pitch2.54mm, F.Cu at (196.5, 105.1)
- added P69: CONN_01X06, lib:6p, F.Cu at (191.4, 96.2)
- added P70: CONN_01X06, lib:6p, F.Cu at (191.4, 116.5)
- added P71: CONN_01X02, lib:2P, F.Cu at (191.4, 73.3)
- added P72: CONN_01X02, lib:2P, F.Cu at (191.4, 126.7)
- added P73: CONN_01X06, lib:6p, F.Cu at (188.9, 96.2)
- added P74: CONN_01X06, lib:6p, F.Cu at (188.9, 116.5)
- added P75: CONN_01X02, lib:2P, F.Cu at (188.9, 73.3)
- added P76: CONN_01X02, lib:2P, F.Cu at (188.9, 126.7)
- added P77: CONN_01X06, lib:6p, F.Cu at (186.4, 96.2)
- added P78: CONN_01X06, lib:6p, F.Cu at (186.4, 116.5)
- added P79: CONN_01X02, lib:2P, F.Cu at (186.4, 73.3)
- added P80: CONN_01X02, lib:2P, F.Cu at (186.4, 126.7)
- added P81: CONN_01X06, lib:6p, F.Cu at (183.8, 96.2)
- added P82: CONN_01X06, lib:6p, F.Cu at (183.8, 116.5)
- added P83: CONN_01X02, lib:2P, F.Cu at (183.8, 73.3)
- added P84: CONN_01X02, lib:2P, F.Cu at (183.8, 126.7)
- added P85: CONN_01X06, lib:6p, F.Cu at (181.3, 96.2)
- added P86: CONN_01X06, lib:6p, F.Cu at (181.3, 116.5)
- added P87: CONN_01X02, lib:2P, F.Cu at (181.3, 73.3)
- added P88: CONN_01X02, lib:2P, F.Cu at (181.3, 126.7)
- added P89: CONN_01X06, lib:6p, F.Cu at (178.7, 96.2)
- added P90: CONN_01X06, lib:6p, F.Cu at (178.7, 116.5)
- added P91: CONN_01X02, lib:2P, F.Cu at (178.7, 73.3)
- added P92: CONN_01X02, lib:2P, F.Cu at (178.7, 126.7)
- added P93: CONN_01X06, lib:6p, F.Cu at (176.2, 96.2)
- added P94: CONN_01X06, lib:6p, F.Cu at (176.2, 116.5)
- added P95: CONN_01X02, lib:2P, F.Cu at (176.2, 73.3)
- added P96: CONN_01X02, lib:2P, F.Cu at (176.2, 126.7)
- added P97: CONN_01X06, lib:6p, F.Cu at (173.7, 96.2)
- added P98: CONN_01X06, lib:6p, F.Cu at (173.7, 116.5)
- added P99: CONN_01X02, lib:2P, F.Cu at (173.7, 73.3)
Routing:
- net Net-(JP177-Pad2): track 55.2 -> 54.5 mm
